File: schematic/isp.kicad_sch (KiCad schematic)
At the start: 1 part, among them J5 AVR_ISP_not_isolated_from_mai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

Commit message: Update schematics
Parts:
- renumbered J5 to J6
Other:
- title: In System Programmer port - WARNING not isolated -> Motor RPM controller - ISP - WARNING not isolated
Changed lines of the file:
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@@
 	(paper "A4")
 	(title_block
-		(title "In System Programmer port - WARNING not isolated")
-		(date "2024-08-21")
+		(title "Motor RPM controller - ISP - WARNING not isolated")
+		(date "2025-09-01")
 		(rev "1.0")
 		(company "Michael Büsch <m@bues.ch>")
@@
 		(dnp no)
 		(fields_autoplaced yes)
-		(property "Reference" "J5"
+		(property "Reference" "J6"
 			(at 147.32 118.11 0)
 			(effects
@@
 			(project ""
 				(path "/167e0419-9f88-4ea4-ae96-d03af9cd26b8/c3fe41b2-b1c4-4cc7-8832-2a133fbf9896"
-					(reference "J5")
+					(reference "J6")
 					(unit 1)
 				)

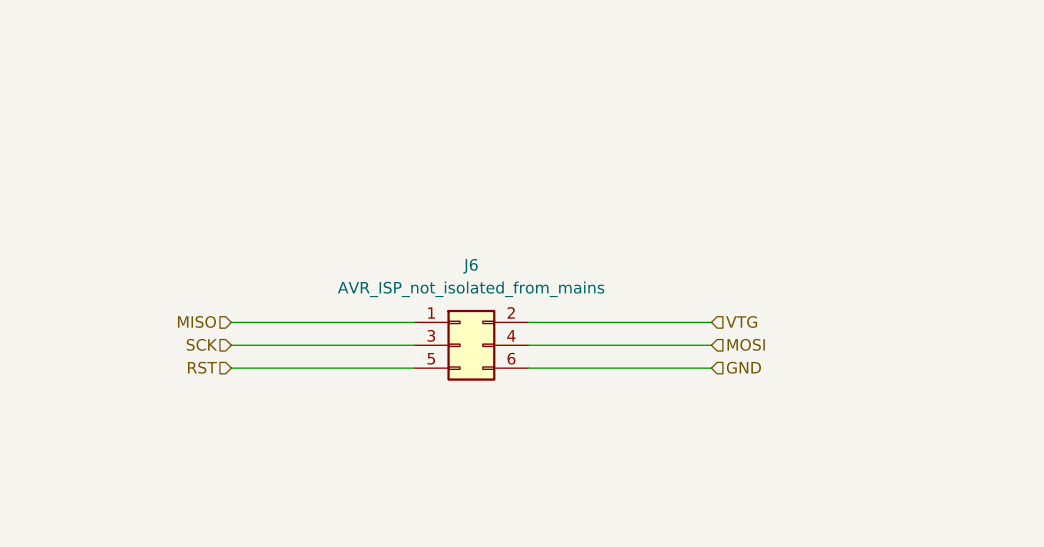
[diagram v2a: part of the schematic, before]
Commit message: schematic: Add DW pinheader
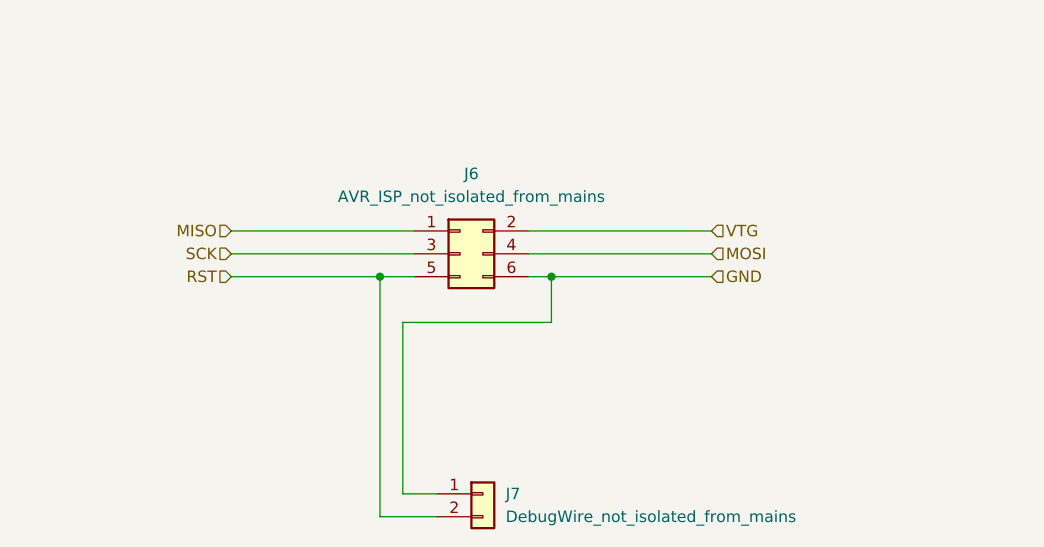
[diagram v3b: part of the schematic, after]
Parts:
- added J7: DebugWire_not_isolated_from_mains, symbol Connector_Generic:Conn_01x02
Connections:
- net GND: now also J7.1 (Pin_1)
- net RST: now also J7.2 (Pin_2)
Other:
- moved on the sheet: J6
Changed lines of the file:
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@@
 		)
 	)
-	(wire
-		(pts
-			(xy 153.67 129.54) (xy 173.99 129.54)
-		)
-		(stroke
-			(width 0)
-			(type default)
-		)
-	)
-	(wire
-		(pts
-			(xy 120.65 129.54) (xy 140.97 129.54)
-		)
-		(stroke
-			(width 0)
-			(type default)
-		)
-	)
-	(wire
-		(pts
-			(xy 120.65 124.46) (xy 140.97 124.46)
-		)
-		(stroke
-			(width 0)
-			(type default)
-		)
-	)
-	(wire
-		(pts
-			(xy 153.67 124.46) (xy 173.99 124.46)
-		)
-		(stroke
-			(width 0)
-			(type default)
-		)
-	)
-	(wire
-		(pts
-			(xy 153.67 127) (xy 173.99 127)
-		)
-		(stroke
-			(width 0)
-			(type default)
-		)
-	)
-	(wire
-		(pts
-			(xy 120.65 127) (xy 140.97 127)
+	(junction
+		(at 156.21 119.38)
+		(diameter 0)
+		(color 0 0 0 0)
+	)
+	(junction
+		(at 137.16 119.38)
+		(diameter 0)
+		(color 0 0 0 0)
+	)
+	(wire
+		(pts
+			(xy 153.67 119.38) (xy 156.21 119.38)
+		)
+		(stroke
+			(width 0)
+			(type default)
+		)
+	)
+	(wire
+		(pts
+			(xy 156.21 119.38) (xy 173.99 119.38)
+		)
+		(stroke
+			(width 0)
+			(type default)
+		)
+	)
+	(wire
+		(pts
+			(xy 120.65 119.38) (xy 137.16 119.38)
+		)
+		(stroke
+			(width 0)
+			(type default)
+		)
+	)
+	(wire
+		(pts
+			(xy 137.16 119.38) (xy 140.97 119.38)
+		)
+		(stroke
+			(width 0)
+			(type default)
+		)
+	)
+	(wire
+		(pts
+			(xy 156.21 119.38) (xy 156.21 124.46)
+		)
+		(stroke
+			(width 0)
+			(type default)
+		)
+	)
+	(wire
+		(pts
+			(xy 137.16 119.38) (xy 137.16 146.05)
+		)
+		(stroke
+			(width 0)
+			(type default)
+		)
+	)
+	(wire
+		(pts
+			(xy 139.7 124.46) (xy 139.7 143.51)
+		)
+		(stroke
+			(width 0)
+			(type default)
+		)
+	)
+	(wire
+		(pts
+			(xy 156.21 124.46) (xy 139.7 124.46)
+		)
+		(stroke
+			(width 0)
+			(type default)
+		)
+	)
+	(wire
+		(pts
+			(xy 139.7 143.51) (xy 143.51 143.51)
+		)
+		(stroke
+			(width 0)
+			(type default)
+		)
+	)
+	(wire
+		(pts
+			(xy 143.51 146.05) (xy 137.16 146.05)
+		)
+		(stroke
+			(width 0)
+			(type default)
+		)
+	)
+	(wire
+		(pts
+			(xy 120.65 114.3) (xy 140.97 114.3)
+		)
+		(stroke
+			(width 0)
+			(type default)
+		)
+	)
+	(wire
+		(pts
+			(xy 153.67 114.3) (xy 173.99 114.3)
+		)
+		(stroke
+			(width 0)
+			(type default)
+		)
+	)
+	(wire
+		(pts
+			(xy 153.67 116.84) (xy 173.99 116.84)
+		)
+		(stroke
+			(width 0)
+			(type default)
+		)
+	)
+	(wire
+		(pts
+			(xy 120.65 116.84) (xy 140.97 116.84)
 		)
 		(stroke
@@
 	(hierarchical_label "MISO"
 		(shape input)
-		(at 120.65 124.46 180)
+		(at 120.65 114.3 180)
 		(effects
 			(font
@@
 	(hierarchical_label "GND"
 		(shape input)
-		(at 173.99 129.54 0)
+		(at 173.99 119.38 0)
 		(effects
 			(font
@@
 	(hierarchical_label "SCK"
 		(shape input)
-		(at 120.65 127 180)
+		(at 120.65 116.84 180)
 		(effects
 			(font
@@
 	(hierarchical_label "VTG"
 		(shape input)
-		(at 173.99 124.46 0)
+		(at 173.99 114.3 0)
 		(effects
 			(font
@@
 	(hierarchical_label "MOSI"
 		(shape input)
-		(at 173.99 127 0)
+		(at 173.99 116.84 0)
 		(effects
 			(font
@@
 	(hierarchical_label "RST"
 		(shape input)
-		(at 120.65 129.54 180)
+		(at 120.65 119.38 180)
 		(effects
 			(font
@@
 			)
 			(justify right)
+		)
+	)
+	(symbol
+		(lib_id "Connector_Generic:Conn_01x02")
+		(at 148.59 143.51 0)
+		(unit 1)
+		(exclude_from_sim no)
+		(in_bom yes)
+		(on_board yes)
+		(dnp no)
+		(fields_autoplaced yes)
+		(property "Reference" "J7"
+			(at 151.13 143.5099 0)
+			(effects
+				(font
+					(size 1.27 1.27)
+				)
+				(justify left)
+			)
+		)
+		(property "Value" "DebugWire_not_isolated_from_mains"
+			(at 151.13 146.0499 0)
+			(effects
+				(font
+					(size 1.27 1.27)
+				)
+				(justify left)
+			)
+		)
+		(property "Footprint" ""
+			(at 148.59 143.51 0)
+			(effects
+				(font
+					(size 1.27 1.27)
+				)
+				(hide yes)
+			)
+		)
+		(property "Datasheet" "~"
+			(at 148.59 143.51 0)
+			(effects
+				(font
+					(size 1.27 1.27)
+				)
+				(hide yes)
+			)
+		)
+		(property "Description" "Generic connector, single row, 01x02, script generated (kicad-library-utils/schlib/autogen/connector/)"
+			(at 148.59 143.51 0)
+			(effects
+				(font
+					(size 1.27 1.27)
+				)
+				(hide yes)
+			)
+		)
+		(pin "1"
+		)
+		(pin "2"
+		)
+		(instances
+			(project ""
+				(path "/167e0419-9f88-4ea4-ae96-d03af9cd26b8/c3fe41b2-b1c4-4cc7-8832-2a133fbf9896"
+					(reference "J7")
+					(unit 1)
+				)
+			)
 		)
 	)
 	(symbol
 		(lib_id "Connector_Generic:Conn_02x03_Odd_Even")
-		(at 146.05 127 0)
+		(at 146.05 116.84 0)
 		(unit 1)
 		(exclude_from_sim no)
@@
 		(fields_autoplaced yes)
 		(property "Reference" "J6"
-			(at 147.32 118.11 0)
+			(at 147.32 107.95 0)
 			(effects
 				(font
@@
 		)
 		(property "Value" "AVR_ISP_not_isolated_from_mains"
-			(at 147.32 120.65 0)
+			(at 147.32 110.49 0)
 			(effects
 				(font
@@
 		)
 		(property "Footprint" ""
-			(at 146.05 127 0)
+			(at 146.05 116.84 0)
 			(effects
 				(font
@@
 		)
 		(property "Datasheet" "~"
-			(at 146.05 127 0)
+			(at 146.05 116.84 0)
 			(effects
 				(font
@@
 		)
 		(property "Description" "Generic connector, double row, 02x03, odd/even pin numbering scheme (row 1 odd numbers, row 2 even numbers), script generated (kicad-library-utils/schlib/autogen/connector/)"
-			(at 146.05 127 0)
-			(effects
-				(font
+			(at 146.05 116.84 0)
+			(effects
+				(font

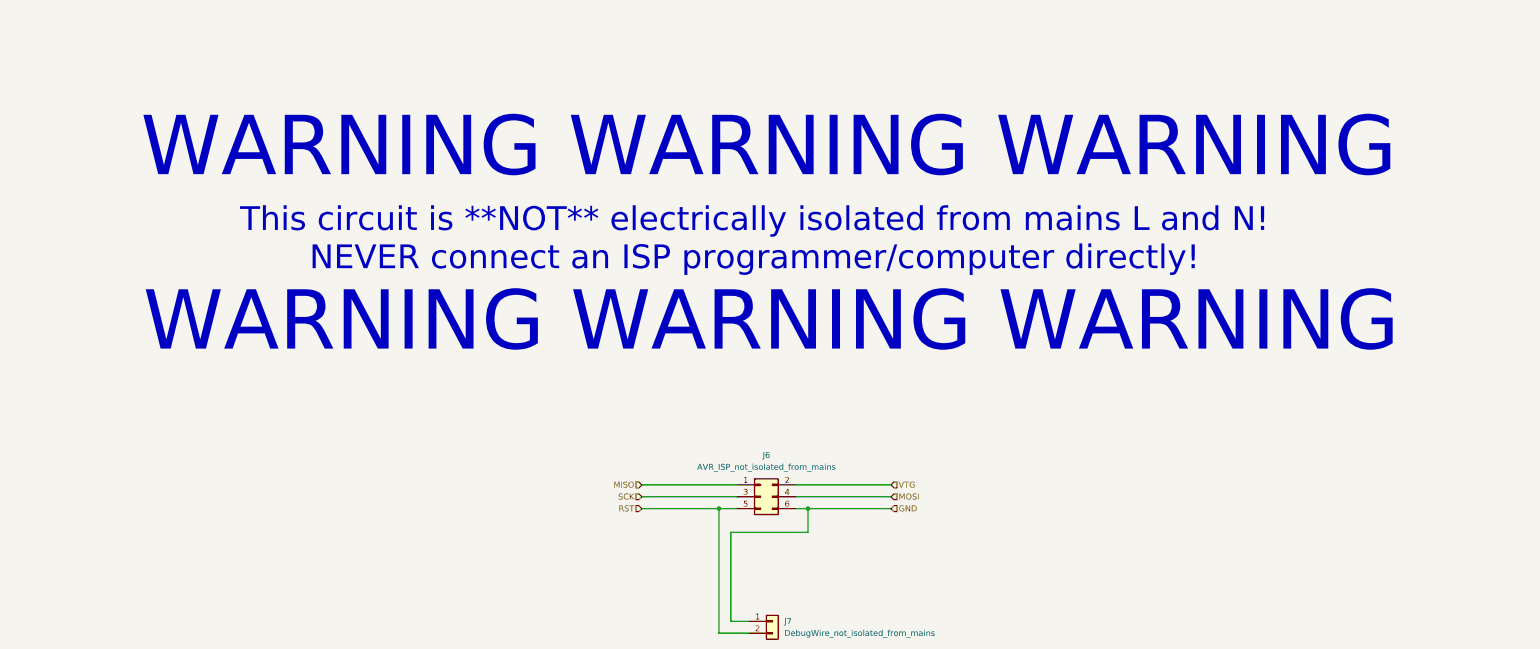
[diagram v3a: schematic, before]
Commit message: schematic: Update trig resistor
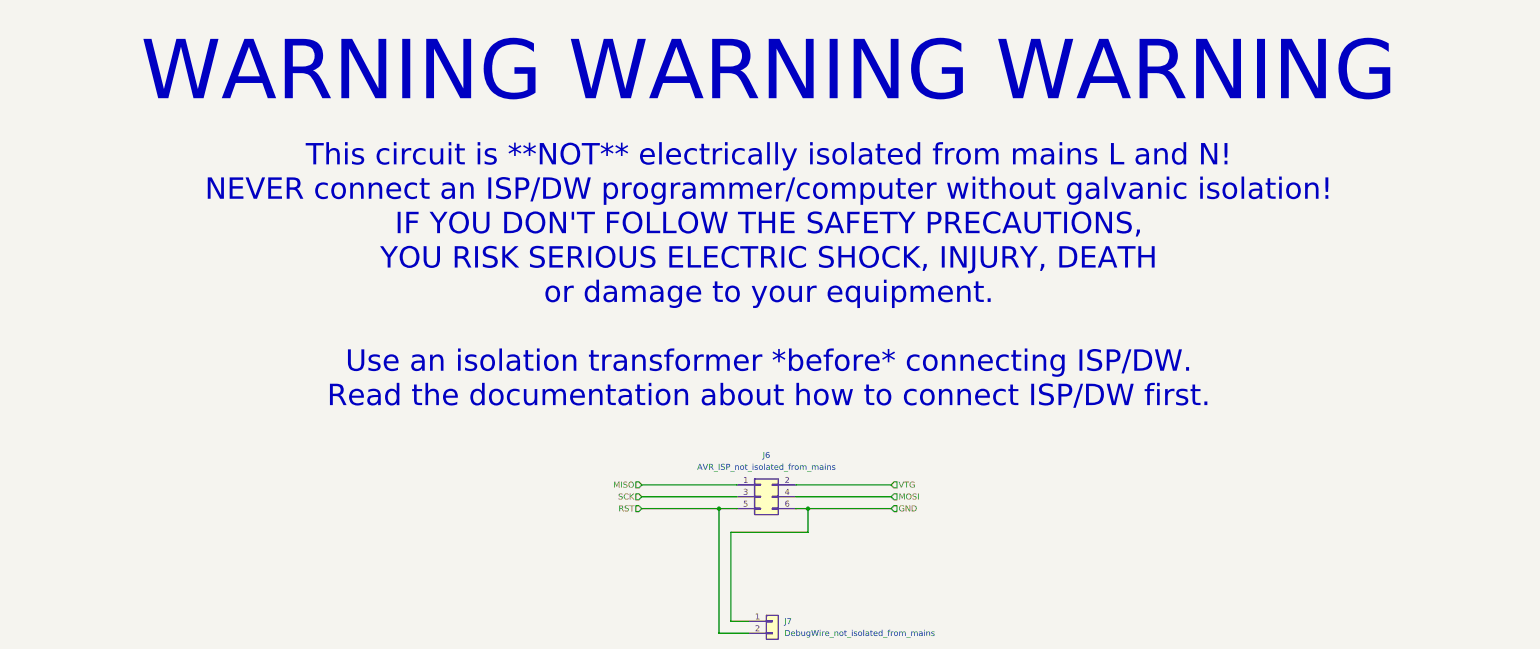
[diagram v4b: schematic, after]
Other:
- note added: "This circuit is **NOT** electrically isolated from mains L and N! NEVER connect an ISP/DW programmer/computer without galvanic isolation! IF YOU DON'T FOLLOW THE SAFETY PRECAUTIONS, YOU RISK SERIOUS ELECTRIC SHOCK, INJURY, DEATH or damage to your equipment. Use an isolation transformer *before* connecting ISP/DW. Read the documentation about how to connect ISP/DW first."
- note removed: "This circuit is **NOT** electrically isolated from mains L and N! NEVER connect an ISP programmer/computer directly!"
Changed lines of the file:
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@@
 	(text "WARNING WARNING WARNING"
 		(exclude_from_sim no)
-		(at 147.828 42.164 0)
+		(at 147.828 25.908 0)
 		(effects
 			(font
@@
 		)
 	)
-	(text "This circuit is **NOT** electrically isolated from mains L and N!\nNEVER connect an ISP programmer/computer directly!"
+	(text "This circuit is **NOT** electrically isolated from mains L and N!\nNEVER connect an ISP/DW programmer/computer without galvanic isolation!\nIF YOU DON'T FOLLOW THE SAFETY PRECAUTIONS,\nYOU RISK SERIOUS ELECTRIC SHOCK, INJURY, DEATH\nor damage to your equipment.\n\nUse an isolation transformer *before* connecting ISP/DW.\nRead the documentation about how to connect ISP/DW first."
 		(exclude_from_sim no)
-		(at 144.78 61.722 0)
+		(at 147.828 69.596 0)
 		(effects
 			(font
-				(size 5.08 5.08)
+				(size 4.572 4.572)
 			)
 		)
-	)
-	(text "WARNING WARNING WARNING"
-		(exclude_from_sim no)
-		(at 148.336 79.502 0)
-		(effects
-			(font
-				(size 12.7 12.7)
-			)
-		)
